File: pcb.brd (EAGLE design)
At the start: 87.3 x 59 mm, 57 parts, among them U2 ISO7221A_D_8, U3 MAX232E_D_16, U4 ISO7221A_D_8, U5 DCH010505S_EDJ_4, U6 REG101-3_DBV_5, U7 DCH010505S_EDJ_4, U8 MSP430G2553_PW_28

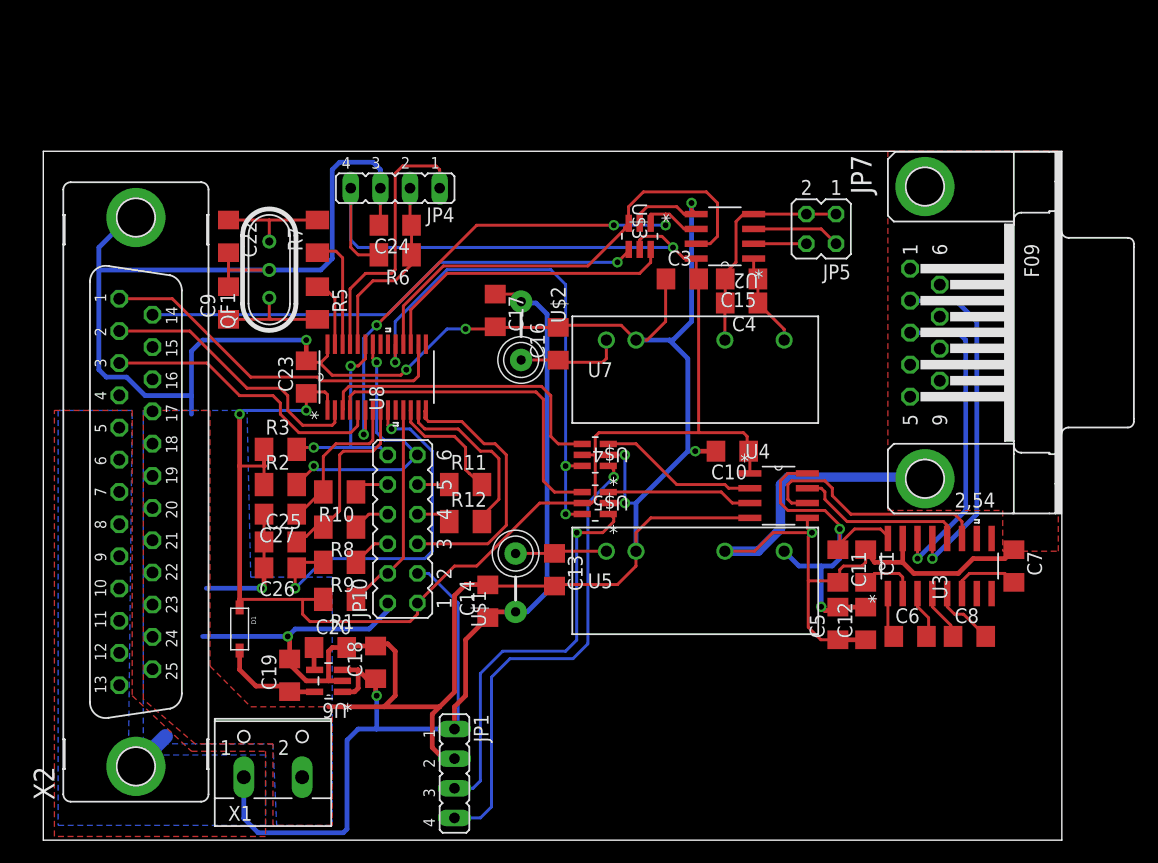
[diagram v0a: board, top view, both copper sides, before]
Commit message: Updated UART and expansion plug
Moved to true dual UART (one timer based)
Added remaining unused pins to expansion plug
finished first draft routing...no DRC check
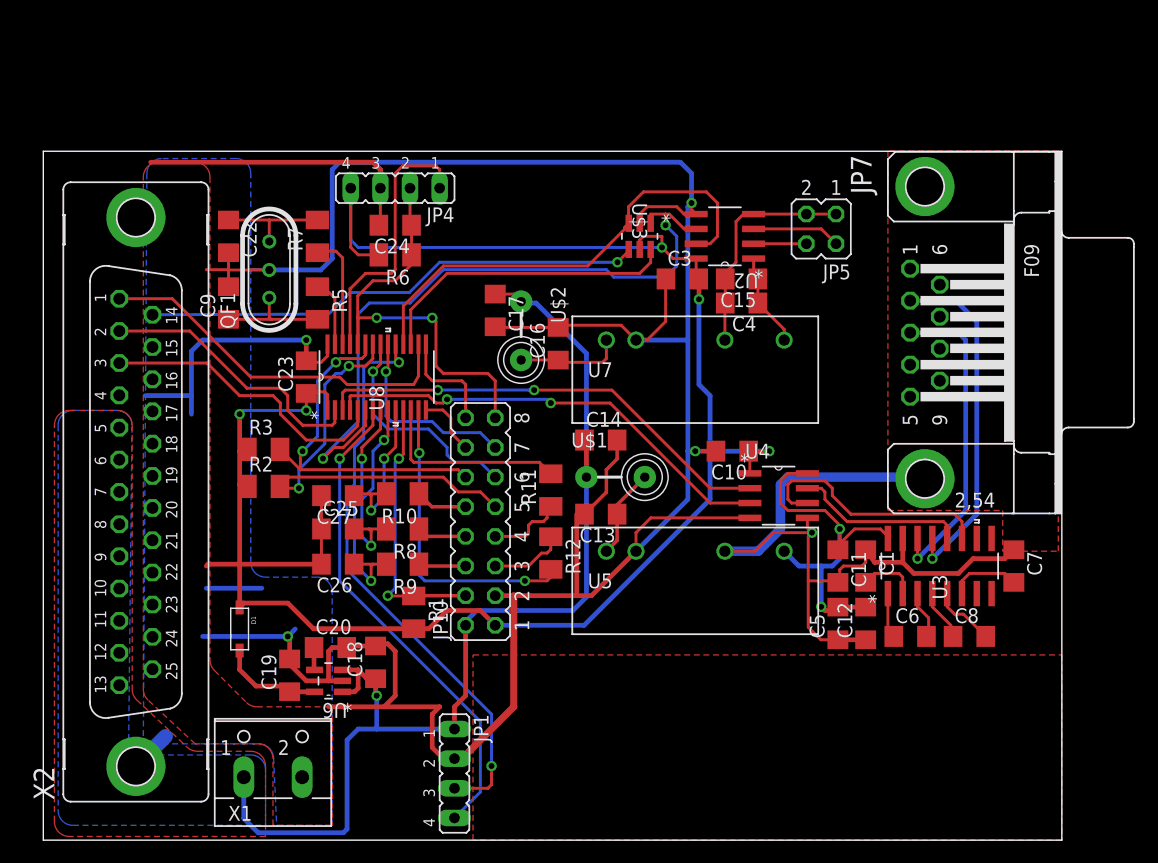
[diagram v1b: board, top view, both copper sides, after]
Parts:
- removed U$4, U$5: TS5A3159-Q1, TI:DBV6
- JP10: device jumper:JP6Q -> jumper:JP8Q
- moved C14 16.9 mm to (47.8, 34.3), turned to 0 degrees
- moved U$1 12.5 mm to (49.1, 31.1), turned to 0 degrees
- moved R12 7.79 mm to (43.5, 24.6), turned to 270 degrees
- moved R11 7.32 mm to (43.5, 30.0), turned to 90 degrees
- moved JP10 6.70 mm to (37.5, 27.3)
- moved R1 6.45 mm to (31.8, 19.5), turned to 270 degrees
- moved C13 6.20 mm to (47.8, 27.9), turned to 180 degrees
- moved R10 5.40 mm to (30.8, 29.7)
- moved R8 5.40 mm to (30.8, 26.7)
- moved R9 5.40 mm to (30.8, 23.7)
- moved C27 5.17 mm to (25.2, 29.5)
- moved C25 5.05 mm to (25.2, 26.7)
- moved C26 4.93 mm to (25.2, 23.7)
- moved R2 1.44 mm to (18.9, 30.3)
- moved R3 1.43 mm to (18.9, 33.5)
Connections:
- removed net RX: U$4.4, U8.3
- removed net TX: U$5.4, U8.4
- removed net UART_MODE: U$4.6, U$5.6, U8.19
- new net GPIO1: JP10.11, U8.21
- new net GPIO2: JP10.13, U8.20
- new net GPIO3: JP10.16, U8.15
- net ENCODER_A_MCU: now also U8.10; no longer U8.7
- net ENCODER_B_MCU: now also C25.2, R8.2; no longer C26.1, R9.2
- net ENCODER_PUSH: now also C26.1, R9.2; no longer C25.2, R8.2
- net GND: now also JP10.3; no longer JP10.2, U$4.2, U$5.2
- net LASER_ON: now also JP10.14; no longer JP10.5
- net N$18: now also JP10.7; no longer JP10.9
- net N$19: now also JP10.5; no longer JP10.7
- net RST: now also JP10.15
- net RX1: now also U8.3; no longer U$4.3
- net RX2: now also U8.7; no longer U$4.1
- net SCL: now also JP10.9; no longer JP10.11
- net TX1: now also U8.4; no longer U$5.3
- net TX2: now also U8.19; no longer U$5.1
- net VCC_3V: no longer U$4.5, U$5.5
- net VCC_5V: now also JP10.2; no longer JP10.3
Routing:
- net UART_MODE: track 45.2 -> 0.00 mm, vias 3 -> 0
- net TX: track 28.9 -> 0.00 mm
- net TX1: track 12.5 -> 39.5 mm, vias 0 -> 2
- net RX: track 26.3 -> 0.00 mm
- net RX1: track 13.7 -> 40.0 mm, vias 0 -> 2
- net RST: track 16.5 -> 35.9 mm, vias 0 -> 2
- net GPIO1: track 0.00 -> 19.3 mm, vias 0 -> 1
- net LASER_ON: track 23.3 -> 5.48 mm
- net GPIO2: track 0.00 -> 16.7 mm, vias 0 -> 1
- net ENCODER_B_MCU: track 32.0 -> 17.1 mm
- net TX2: track 34.8 -> 49.6 mm, vias 1 -> 2
- net SCL: track 23.7 -> 37.7 mm
- net SDA: track 17.9 -> 31.1 mm
- net TTL_IN: track 46.5 -> 59.4 mm, vias 4 -> 2
- net GND: track 288.2 -> 300.9 mm, vias 9 -> 4
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
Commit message: updated layout and board
Fixed interlock design
Added analog front end to analog inputs
changed MCU to MSP450 5 series
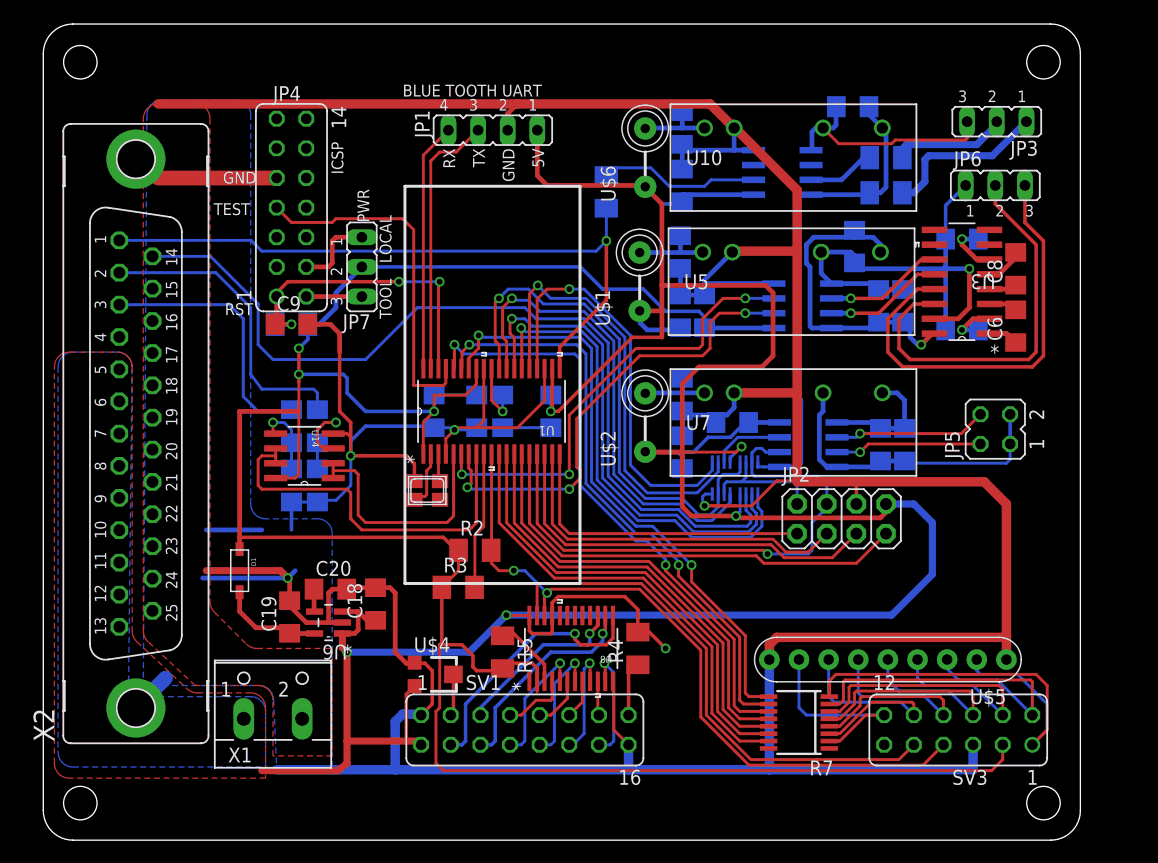
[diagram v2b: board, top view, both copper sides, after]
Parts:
- removed C22, C23, C24, C25, C26, C27: (no value), adafruit:C1206
- removed JP10: (no value), jumper:JP8Q
- removed QF1: 10G7A-12.5KHZ, crystal:HC49U
- removed R12: (no value), adafruit:M1206
- removed U$3: TS5A3159-Q1, TI:DBV6
- added C2, C29: 2.2 uF, adafruit:C1206
- added C30: 4.7 uF, adafruit:C1206
- added C31, C32, C33, C34: 0.1 uF, adafruit:C1206
- added JP2: (no value), adafruit:2X04
- added JP3, JP6: (no value), jumper:JP2
- added Q2: (no value), adafruit:NX3225
- added R14: 500k, adafruit:M1206
- added R15: 10k, adafruit:M1206
- added R4: (no value), adafruit:M1206
- added SV1: (no value), con-lsta:FE08-2
- added SV3: (no value), con-lsta:FE06-2
- added U$4: 10k, adafruit:TC33X
- added U$5: 100 nF, TI:SIP9
- added U$6: 3 uH, adafruit:FB
- added U1: MSP430F5172_DA_38, TI:DA38
- added U10: DCH010505S_EDJ_4, TI:EDJ4
- added U11: ISO7221A_D_8, TI:D8
- added U12, U13: TS5A3357_DCU_8, TI:DCU8
- added U14: TLV2242_D_8, TI:D8
- C1, C6, C7, C8: value (none) -> 1 uF
- C10, C11, C12, C18, C19, C3, C4: value (none) -> 0.1 uF
- C13, C16: value (none) -> 2.2 uF
- C14, C17: value (none) -> 4.7 uF
- C15, C5: value (none) -> 10 uF
- C20: value (none) -> 0.01 uF
- C9: value (none) -> 2.2 nF
- JP4: device jumper:JP4 -> con-lsta:FE07-2
- JP7: device con-subd:F09HP -> jumper:JP2
- R1: value (none) -> 1M; device adafruit:M1206 -> adafruit:R1206
- R10: value (none) -> 47k
- R11: value (none) -> 750k
- R2, R3: value (none) -> 43k
- R5: value (none) -> 500k
- R6: value (none) -> 0R; device adafruit:M1206 -> adafruit:R1206
- R7: value (none) -> 100k; device adafruit:M1206 -> resistor-bourns:2QSP16
- R8: value (none) -> 600k; device adafruit:M1206 -> adafruit:R1206
- R9: value (none) -> 400k; device adafruit:M1206 -> adafruit:R1206
- U$1, U$2: value FB -> 3 uH
- U6: device TI:DBV5 -> TI:DBV5@1
- U8: value MSP430G2553_PW_28 -> TCA6416A_PW_24; device TI:PW28 -> TI:PW24
- moved R7 58.7 mm to (64.8, 10.1)
- moved JP1 55.2 mm to (38.5, 60.9), turned to 180 degrees
- moved R5 50.3 mm to (72.2, 58.5), flipped to the bottom, turned to 0 degrees
- moved JP7 48.6 mm to (27.3, 49.1)
- moved C8 31.8 mm to (83.3, 49.0), turned to 90 degrees
- moved U8 28.6 mm to (45.2, 16.4)
- moved C7 28.4 mm to (78.7, 51.5), flipped to the bottom, turned to 180 degrees
- moved C6 28.1 mm to (83.3, 44.1), turned to 90 degrees
- moved C5 27.8 mm to (73.7, 45.8), flipped to the bottom, turned to 270 degrees
- moved C11 27.4 mm to (69.5, 50.9), flipped to the bottom
- moved C12 27.2 mm to (71.6, 45.8), flipped to the bottom, turned to 270 degrees
- moved U5 26.9 mm to (71.8, 45.3)
- moved R11 26.0 mm to (48.3, 55.6), flipped to the bottom, turned to 270 degrees
- moved U3 24.4 mm to (78.7, 47.9), turned to 180 degrees
- moved C13 23.5 mm to (54.6, 50.4), flipped to the bottom, turned to 270 degrees
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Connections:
- net N$20 renamed SERIAL_VCC
- removed net ENCODER_A_MCU: C27.1, R10.2, U8.10
- removed net ENCODER_B_MCU: C25.2, R8.2, U8.9
- removed net ENCODER_PUSH: C26.1, R9.2, U8.8
- removed net GPIO1: JP10.11, U8.21
- removed net GPIO2: JP10.13, U8.20
- removed net GPIO3: JP10.16, U8.15
- removed net LASER_ENABLE: U8.16, X2.1
- removed net LASER_ILK_LED: R11.2, U8.12
- removed net LASER_ON: JP10.14, U8.14
- removed net LASER_ON_LED: R12.2, U8.13
- removed net MCU_TTL: U$3.3, U2.7, U8.18
- removed net N$16: C22.1, QF1.3, R7.2
- removed net N$19: JP10.5, R12.1
- removed net TTL_CTL: U$3.6, U8.17
- new net 3VIO-0: R7.15, U1.11
- new net 3VIO-0H: R7.8, SV3.1, U$5.1
- new net 3VIO-1: R7.14, U1.12
- new net 3VIO-1H: R7.7, SV3.2, U$5.2
- new net 3VIO-2: R7.13, U1.13
- new net 3VIO-2H: R7.6, SV3.4, U$5.3
- new net 3VIO-3: R7.12, U1.14
- new net 3VIO-3H: R7.5, SV3.6, U$5.4
- new net 3VIO-4: R7.11, U1.34
- new net 3VIO-4H: R7.4, SV3.8, U$5.5
- new net 3VIO-5: R7.10, U1.33
- new net 3VIO-5H: R7.3, SV3.10, U$5.6
- new net 3VIO-6: R7.9, U1.32
- new net 3VIO-6H: R7.2, SV3.12, U$5.7
- new net 5VIO-0: JP2.7, U1.15
- new net 5VIO-1: JP2.5, U1.17
- new net 5VIO-2: JP2.3, U1.18
- new net 5VIO-3: JP2.1, U1.19
- new net CONTRAST: SV1.3, U$4.2
- new net DB0: SV1.7, U8.4
- new net DB1: SV1.8, U8.5
- new net DB2: SV1.9, U8.6
- new net DB3: SV1.10, U8.7
- new net DB4: SV1.11, U8.8
- new net DB5: SV1.12, U8.9
- new net DB6: SV1.13, U8.10
- new net DB7: SV1.14, U8.11
- new net ENABLE: SV1.6, U8.14
- new net EXT_SRC-A: U1.24, U13.6
- new net EXT_SRC-B: U1.23, U13.5
- new net EXT_TTL: JP2.2, U12.2, U13.2
- new net G2: Q2.2
- new net ITL_POWER: C29.1, U$6.P$2, U10.1
- new net LASER_CURRENT_3V: U1.5, U14.1, U14.2
- new net LASER_ILK_HIGH: R11.1, U11.2
- new net LASER_SRC-A: U1.26, U12.6
- new net LASER_SRC-B: U1.25, U12.5
- new net LASER_TEMPERATURE_3V: U1.8, U14.6, U14.7
- new net MCU_TTL1: U1.28, U12.1, U13.3
- new net MCU_TTL2: U1.27, U13.1
- new net N$21: Q2.1, U1.2
- new net N$22: Q2.3, U1.3
- new net N$24: C34.1, U1.29
- new net N$27: C2.1, R14.2, U10.4, U11.8
- new net N$28: C2.2, JP3.3, U10.3, U11.5
- new net N$35: JP3.1, R14.1
- new net R/W: SV1.5, U8.15
- new net RS: SV1.4, U8.13
- new net TTL_OUT: U13.7, U2.7
- new net VCC_LED: R4.1, SV1.15
- net GND: now also C29.2, C30.2, C31.2, C32.2, C33.2, C34.2, JP2.6, JP4.9, Q2.4, R1.1, R8.1, SV1.1, SV1.16, SV3.5, U$4.1, U$5.BUS, U$5.BUS2, U1.22, U1.30, U1.4, U10.2, U11.4, U12.4, U13.4, U14.4, U8.12; no longer C22.2, C23.2, C24.2, C25.1, C26.2, C27.2, JP10.3, JP4.3, QF1.2, U$3.2, U8.28
- net LASER_CURRENT: now also R9.2; no longer U8.2
- net LASER_ILK: now also R11.2, U1.20, X2.1; no longer JP10.4, R1.1, U8.11
- net LASER_TEMPERATURE: now also R6.2; no longer U8.5
- net LASER_TTL: now also U12.7; no longer U$3.4
- net N$10: now also R8.2, R9.1, U14.3; no longer JP10.8, R8.1
- net N$12: now also R5.2, U11.7; no longer R5.1, U8.27
- net N$14: now also JP3.2, R5.1; no longer R7.1, U8.26
- net N$15: now also R15.1, U8.3; no longer C9.1, QF1.1, R5.2
- net N$17: now also JP4.2, JP7.3; no longer JP10.10, R10.1
- net N$18: now also JP4.4, JP7.1; no longer JP10.7, R11.1
- net N$8: now also R1.2, R6.1, U14.5; no longer JP10.6, R9.1
- net RS232_RX: now also JP6.3; no longer JP7.2
- net RS232_TX: now also JP6.2; no longer JP7.3
- net RST: now also C9.1, JP4.1, R10.1, U1.36; no longer C24.1, JP10.15, JP4.2, R6.1, U8.24
- net RX1: now also U1.7; no longer U8.3
- net RX2: now also U1.38; no longer U8.7
- net SCL: now also SV3.7, U1.10; no longer JP10.9
- net SDA: now also SV3.9, U1.9; no longer JP10.12
- net SERIAL_GND: now also JP6.1; no longer JP7.5, JP7.G1, JP7.G2
- net TEST: now also JP4.7, U1.35; no longer JP4.1, U8.25
- net TTL_IN: now also JP2.4, U1.16, U12.3; no longer U$3.1, U8.6
- net TX1: now also U1.6; no longer U8.4
- net TX2: now also U1.37; no longer U8.19
- net VCC_3V: now also C31.1, C32.1, JP7.2, R10.2, R15.2, SV3.3, U1.1, U1.31, U14.8, U8.2; no longer C23.1, C3.2, JP10.1, JP4.4, R1.2, R6.2, U$3.5, U2.8, U8.1
- net VCC_5V: now also C3.2, C30.1, C33.1, JP2.8, R4.2, SV1.2, U$4.3, U$6.P$1, U1.21, U11.1, U12.8, U13.8, U2.8, U8.21, U8.24; no longer JP10.2
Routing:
- net VCC_5V: track 96.1 -> 260.7 mm, vias 1 -> 6
- net GND: track 300.9 -> 434.2 mm
- net VCC_3V: track 152.0 -> 208.2 mm, vias 5 -> 3
- net 3VIO-4: track 0.00 -> 52.3 mm, vias 0 -> 2
- net 3VIO-6: track 0.00 -> 51.6 mm, vias 0 -> 2
- net 3VIO-5: track 0.00 -> 51.2 mm, vias 0 -> 2
- net MCU_TTL1: track 0.00 -> 45.8 mm, vias 0 -> 1
- net LASER_SRC-A: track 0.00 -> 42.7 mm, vias 0 -> 1
- net MCU_TTL2: track 0.00 -> 41.7 mm, vias 0 -> 1
- net LASER_SRC-B: track 0.00 -> 41.6 mm, vias 0 -> 1
- net MCU_TTL: track 40.5 -> 0.00 mm
- net 3VIO-0: track 0.00 -> 40.2 mm
- net 3VIO-1: track 0.00 -> 39.2 mm
- net 5VIO-0: track 0.00 -> 39.0 mm
- net EXT_SRC-A: track 0.00 -> 38.5 mm, vias 0 -> 1
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- removed copper zone on layer 1, net SERIAL_GND
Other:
- board size 87.3 x 59 mm -> 88.9 x 70 mm
- board text added: "5V"
- board text added: "BLUE TOOTH UART"
- board text added: "GND"
- board text added: "ICSP"
- board text added: "LOCAL"
- board text added: "PWR"
- board text added: "RST"
- board text added: "RX"
- board text added: "TEST"
- board text added: "TOOL"
- board text added: "TX"

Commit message: Silk Screen and analog front end
Update to documentation on silk screen
Addition of buffered voltage divider for analog front end
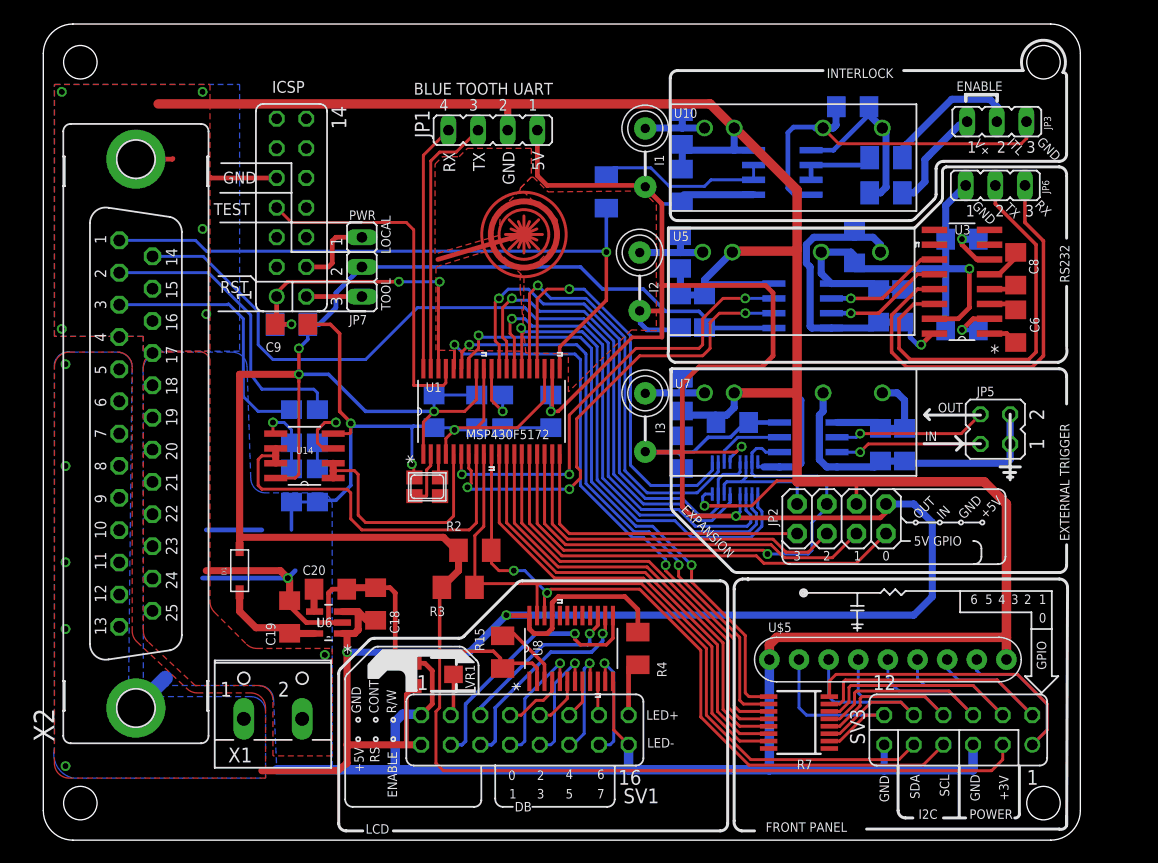
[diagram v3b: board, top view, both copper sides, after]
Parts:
- U1: value MSP430F5172_DA_38 -> MSP430F5172
- U11: value ISO7221A_D_8 -> ISO7420_D_8
- moved Q2 0.32 mm to (32.9, 30.3)
- turned JP3 to 0 degrees
- turned U11 to 0 degrees
- renumbered U$1 to I2, U$2 to I3, U$4 to VR1, U$6 to I1
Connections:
- removed net N$12: R5.2, U11.7
- new net N$19: R5.2, U11.2, U11.3
- net GND: now also SV3.11, U11.8; no longer U11.4
- net LASER_ILK_HIGH: now also U11.6, U11.7; no longer U11.2
- net N$27: now also U11.1; no longer U11.8
- net N$28: now also U11.4; no longer U11.5
- net VCC_5V: now also U11.5; no longer U11.1
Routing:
- net STAR: track 0.00 -> 23.2 mm
- net N$28: track 20.1 -> 33.3 mm
- net N$23: track 0.00 -> 7.61 mm
- net N$19: track 0.00 -> 6.93 mm
- net N$12: track 5.82 -> 0.00 mm
- net N$35: track 14.3 -> 9.19 mm
- net GND: track 434.2 -> 431.2 mm, vias 4 -> 11
- net N$14: track 9.97 -> 12.2 mm
- net VCC_5V: track 260.7 -> 258.9 mm, vias 6 -> 10
- net VCC_3V: track 208.2 -> 209.9 mm
- net 3VIO-1H: track 31.9 -> 30.2 mm
- net N$27: track 14.2 -> 15.6 mm
- net 3VIO-2H: track 29.1 -> 27.8 mm
- net LASER_ILK_HIGH: track 13.8 -> 15.0 mm
- net 3VIO-3H: track 26.0 -> 25.0 mm
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- added copper zone on layer 1, net N$12
- added copper zone on layer 1, net N$16
- added copper zone on layer 1, net N$20
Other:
- board text added: "+3V"
- board text added: "+5V"
- board text added: "0"
- board text added: "1"
- board text added: "2"
- board text added: "3"
- board text added: "4"
- board text added: "5"
- board text added: "5V GPIO"
- board text added: "6"
- board text added: "7"
- board text added: "CONT"
- board text added: "DB"
- board text added: "ENABLE"
- board text added: "EXPANSION"
- board text added: "EXTERNAL TRIGGER"
- board text added: "FRONT PANEL"
- board text added: "GPIO"
- board text added: "I2C"
- board text added: "IN"
- board text added: "INTERLOCK"
- board text added: "ITL"
- board text added: "LCD"
- board text added: "LED+"
- board text added: "LED-"
- board text added: "Laser Current"
- board text added: "Laser Temperature"
- board text added: "OUT"
- board text added: "POWER"
- board text added: "R/W"
- board text added: "RS"
- board text added: "RS232"
- board text added: "SCL"
- board text added: "SDA"
- board text added: "V+"
